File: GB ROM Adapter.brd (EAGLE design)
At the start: 13.3 x 23.5 mm, 7 parts, among them IC1 AM29F016/32

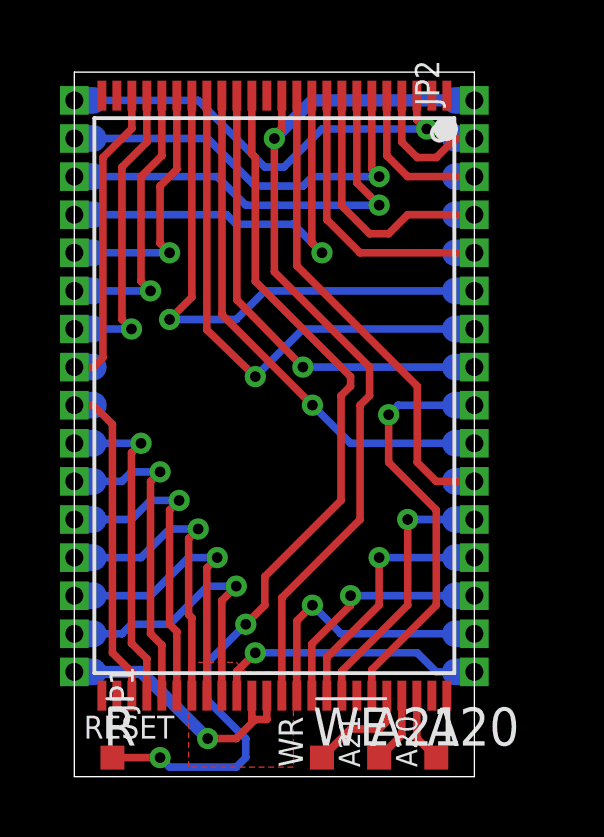
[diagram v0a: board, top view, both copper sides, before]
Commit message: Updated silk screen
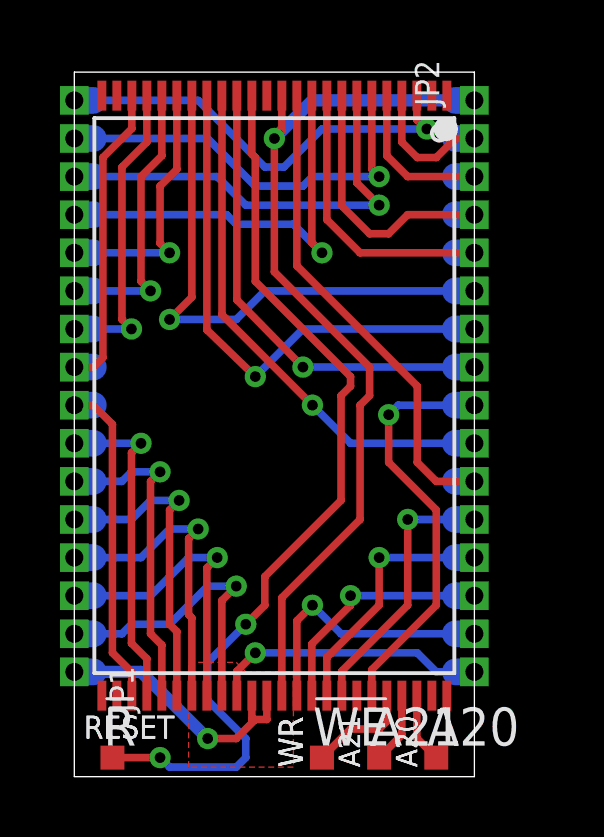
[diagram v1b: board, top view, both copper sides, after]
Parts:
- !R: value TPTP08SQ -> (none)
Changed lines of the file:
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@@
 <?xml version="1.0" encoding="utf-8"?>
 <!DOCTYPE eagle SYSTEM "eagle.dtd">
-<eagle version="6.6.0">
+<eagle version="7.1.0">
 <drawing>
 <settings>
@@
 <layer number="59" name="tCarbon" color="7" fill="1" visible="no" active="no"/>
 <layer number="60" name="bCarbon" color="7" fill="1" visible="no" active="no"/>
-<layer number="90" name="Modules" color="5" fill="1" visible="yes" active="yes"/>
+<layer number="90" name="Modules" color="5" fill="1" visible="no" active="no"/>
 <layer number="91" name="Nets" color="2" fill="1" visible="no" active="no"/>
 <layer number="92" name="Busses" color="1" fill="1" visible="no" active="no"/>
@@
 <vertex x="0.9525" y="21.59"/>
 </polygon>
+<text x="0.3175" y="1.27" size="0.762" layer="25" font="vector" ratio="16">RESET</text>
+<text x="7.62" y="0.3175" size="0.8128" layer="25" font="vector" ratio="16" rot="R90">WR</text>
+<text x="9.525" y="0.3175" size="0.7112" layer="25" font="vector" ratio="16" rot="R90">A21</text>
+<text x="11.43" y="0.3175" size="0.7112" layer="25" font="vector" ratio="16" rot="R90">A20</text>
+<text x="8.255" y="6.0325" size="0.8128" layer="26" font="vector" ratio="16" rot="SMR45">GB ROM ADAPTER
+JRodrigo.net</text>
 </plain>
 <attributes>
@@
 <pass name="Default">
 <param name="RoutingGrid" value="50mil"/>
+<param name="AutoGrid" value="1"/>
+<param name="Efforts" value="0"/>
+<param name="TopRouterVariant" value="1"/>
 <param name="tpViaShape" value="round"/>
 <param name="PrefDir.1" value="|"/>
@@
 <attribute name="TP_SIGNAL_NAME" value="" x="10.16" y="0.635" size="1.778" layer="27" display="off"/>
 </element>
-<element name="!R" library="testpad" package="TP08SQ" value="TPTP08SQ" x="1.27" y="0.635">
+<element name="!R" library="testpad" package="TP08SQ" value="" x="1.27" y="0.635">
 <attribute name="TP_SIGNAL_NAME" value="" x="1.27" y="0.635" size="1.778" layer="27" display="off"/>
 </element>
